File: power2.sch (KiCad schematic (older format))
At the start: 40 parts, among them U3 LMS6002DR2, U4 ECP5

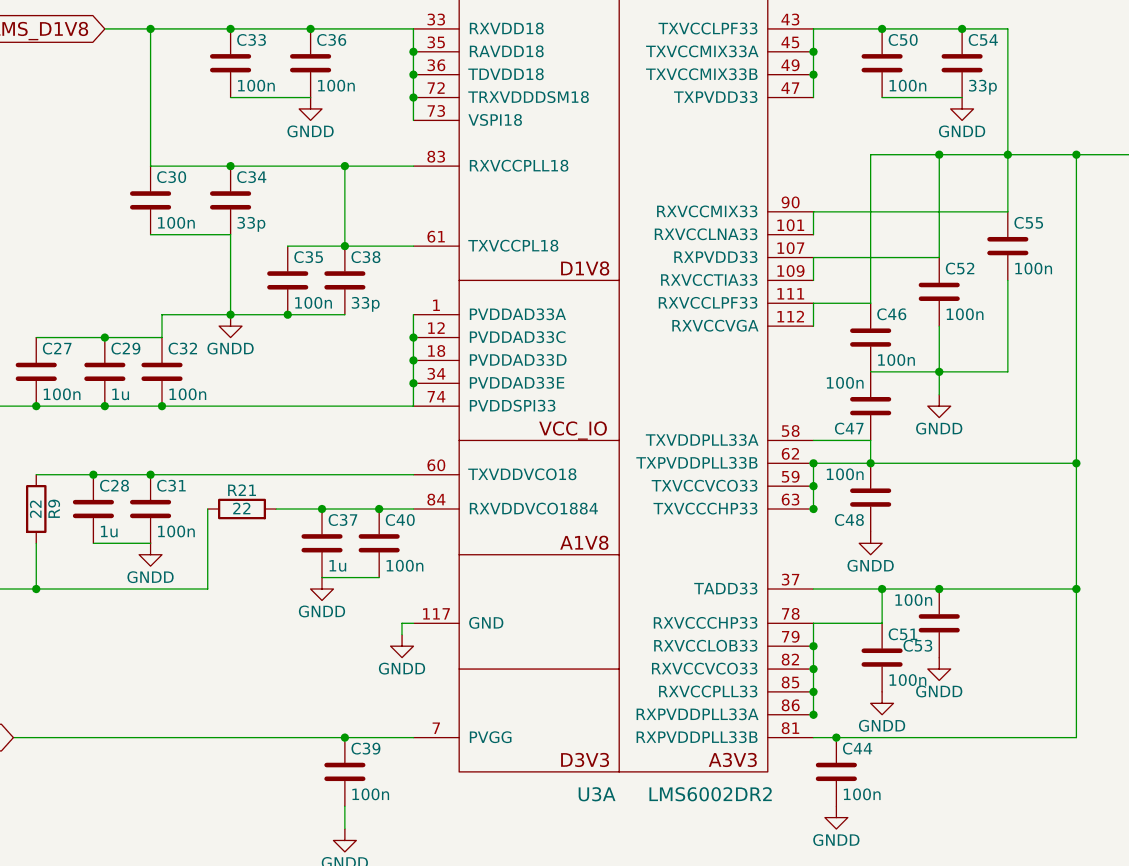
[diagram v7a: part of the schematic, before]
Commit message: Add jumpers for LMS power Traced most nets in LMS digital
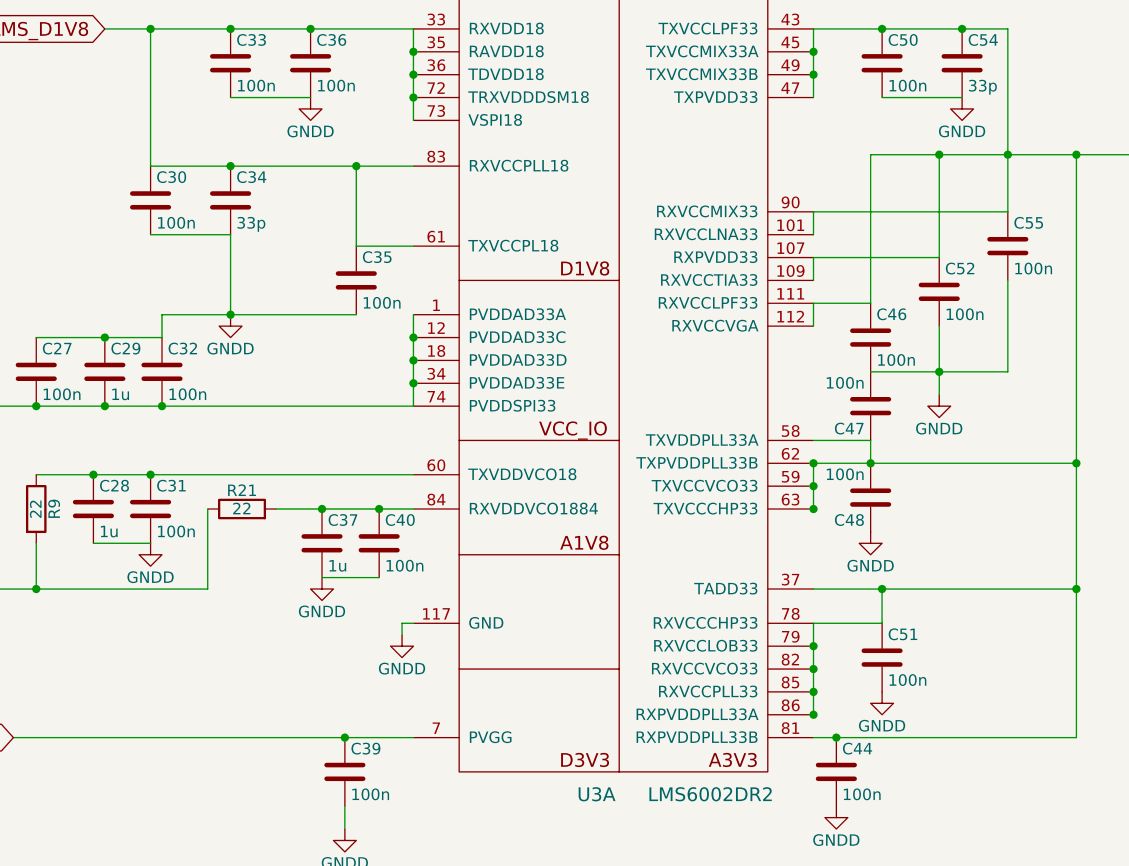
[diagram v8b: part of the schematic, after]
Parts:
- removed C38: 33p, Capacitors_SMD:C_0603, symbol C
- removed C53: 100n, Capacitors_SMD:C_0603, symbol C
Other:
- moved on the sheet: C35
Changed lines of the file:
@@
 Connection ~ 10950 1000
 $Comp
-L GNDD #PWR075
+L GNDD #PWR91
 U 1 1 58A3CB56
 P 10050 6200
-F 0 "#PWR075" H 10050 5950 50  0001 C CNN
+F 0 "#PWR91" H 10050 5950 50  0001 C CNN
 F 1 "GNDD" H 10050 6050 50  0000 C CNN
 F 2 "" H 10050 6200 50  0000 C CNN
@@
 $EndComp
 $Comp
-L +1V1 #PWR076
+L +1V1 #PWR89
 U 1 1 58A3D047
 P 7500 2300
-F 0 "#PWR076" H 7500 2150 50  0001 C CNN
+F 0 "#PWR89" H 7500 2150 50  0001 C CNN
 F 1 "+1V1" H 7500 2440 50  0000 C CNN
 F 2 "" H 7500 2300 50  0000 C CNN
@@
 L C C35
 U 1 1 58A43C62
-P 2500 1950
-F 0 "C35" H 2525 2050 50  0000 L CNN
-F 1 "100n" H 2525 1850 50  0000 L CNN
-F 2 "Capacitors_SMD:C_0603" H 2538 1800 50  0001 C CNN
-F 3 "" H 2500 1950 50  0000 C CNN
-	1    2500 1950
+P 2800 1950
+F 0 "C35" H 2825 2050 50  0000 L CNN
+F 1 "100n" H 2825 1850 50  0000 L CNN
+F 2 "Capacitors_SMD:C_0603" H 2838 1800 50  0001 C CNN
+F 3 "" H 2800 1950 50  0000 C CNN
+	1    2800 1950
 	1    0    0    -1
 $EndComp
@@
 $EndComp
 $Comp
-L C C38
-U 1 1 58A43C77
-P 2750 1950
-F 0 "C38" H 2775 2050 50  0000 L CNN
-F 1 "33p" H 2775 1850 50  0000 L CNN
-F 2 "Capacitors_SMD:C_0603" H 2788 1800 50  0001 C CNN
-F 3 "" H 2750 1950 50  0000 C CNN
-	1    2750 1950
-	1    0    0    -1
-$EndComp
-$Comp
-L GNDD #PWR077
+L GNDD #PWR76
 U 1 1 58A43C7E
 P 2250 2100
-F 0 "#PWR077" H 2250 1850 50  0001 C CNN
+F 0 "#PWR76" H 2250 1850 50  0001 C CNN
 F 1 "GNDD" H 2250 1950 50  0000 C CNN
 F 2 "" H 2250 2100 50  0000 C CNN
@@
 LMS_D1V8
 $Comp
-L GNDD #PWR078
+L GNDD #PWR77
 U 1 1 58A43C85
 P 2600 1150
-F 0 "#PWR078" H 2600 900 50  0001 C CNN
+F 0 "#PWR77" H 2600 900 50  0001 C CNN
 F 1 "GNDD" H 2600 1000 50  0000 C CNN
 F 2 "" H 2600 1150 50  0000 C CNN
@@
 LMS_A1V8
 $Comp
-L GNDD #PWR079
+L GNDD #PWR80
 U 1 1 58A43CCB
 P 3000 3500
-F 0 "#PWR079" H 3000 3250 50  0001 C CNN
+F 0 "#PWR80" H 3000 3250 50  0001 C CNN
 F 1 "GNDD" H 3000 3350 50  0000 C CNN
 F 2 "" H 3000 3500 50  0000 C CNN
@@
 $EndComp
 $Comp
-L GNDD #PWR080
+L GNDD #PWR78
 U 1 1 58A43CD1
 P 2650 3250
-F 0 "#PWR080" H 2650 3000 50  0001 C CNN
+F 0 "#PWR78" H 2650 3000 50  0001 C CNN
 F 1 "GNDD" H 2650 3100 50  0000 C CNN
 F 2 "" H 2650 3250 50  0000 C CNN
@@
 $EndComp
 $Comp
-L GNDD #PWR081
+L GNDD #PWR75
 U 1 1 58A43CD7
 P 1900 3100
-F 0 "#PWR081" H 1900 2850 50  0001 C CNN
+F 0 "#PWR75" H 1900 2850 50  0001 C CNN
 F 1 "GNDD" H 1900 2950 50  0000 C CNN
 F 2 "" H 1900 3100 50  0000 C CNN
@@
 $EndComp
 $Comp
-L GNDD #PWR082
+L GNDD #PWR85
 U 1 1 58A43CEB
 P 5450 1150
-F 0 "#PWR082" H 5450 900 50  0001 C CNN
+F 0 "#PWR85" H 5450 900 50  0001 C CNN
 F 1 "GNDD" H 5450 1000 50  0000 C CNN
 F 2 "" H 5450 1150 50  0000 C CNN
@@
 $EndComp
 $Comp
-L GNDD #PWR083
+L GNDD #PWR79
 U 1 1 58A43D15
 P 2750 4350
-F 0 "#PWR083" H 2750 4100 50  0001 C CNN
+F 0 "#PWR79" H 2750 4100 50  0001 C CNN
 F 1 "GNDD" H 2750 4200 50  0000 C CNN
 F 2 "" H 2750 4350 50  0000 C CNN
@@
 $EndComp
 $Comp
-L GNDD #PWR084
+L GNDD #PWR84
 U 1 1 58A43D1B
 P 5350 2450
-F 0 "#PWR084" H 5350 2200 50  0001 C CNN
+F 0 "#PWR84" H 5350 2200 50  0001 C CNN
 F 1 "GNDD" H 5350 2300 50  0000 C CNN
 F 2 "" H 5350 2450 50  0000 C CNN
@@
 $EndComp
 $Comp
-L GNDD #PWR085
+L GNDD #PWR82
 U 1 1 58A43D2F
 P 5050 3050
-F 0 "#PWR085" H 5050 2800 50  0001 C CNN
+F 0 "#PWR82" H 5050 2800 50  0001 C CNN
 F 1 "GNDD" H 5050 2900 50  0000 C CNN
 F 2 "" H 5050 3050 50  0000 C CNN
@@
 	1    0    0    -1
 $EndComp
-$Comp
-L C C53
-U 1 1 58A43D35
-P 5350 3450
-F 0 "C53" H 5375 3550 50  0000 L CNN
-F 1 "100n" H 5375 3350 50  0000 L CNN
-F 2 "Capacitors_SMD:C_0603" H 5388 3300 50  0001 C CNN
-F 3 "" H 5350 3450 50  0000 C CNN
-	1    5350 3450
-	-1   0    0    1
-$EndComp
 Wire Wire Line
 	1900 1450 3050 1450
 Connection ~ 2250 1450
 Wire Wire Line
-	2500 1800 3050 1800
-Connection ~ 2750 1800
-Wire Wire Line
-	1950 2100 2750 2100
+	1950 2100 2800 2100
 Wire Wire Line
 	2250 2100 2250 1750
-Connection ~ 2500 2100
 Wire Wire Line
 	2250 1750 1900 1750
@@
 	4800 3300 5950 3300
 Connection ~ 5950 2750
-Connection ~ 5350 3300
-$Comp
-L GNDD #PWR086
-U 1 1 58A43D94
-P 5350 3600
-F 0 "#PWR086" H 5350 3350 50  0001 C CNN
-F 1 "GNDD" H 5350 3450 50  0000 C CNN
-F 2 "" H 5350 3600 50  0000 C CNN
-F 3 "" H 5350 3600 50  0000 C CNN
-	1    5350 3600
-	1    0    0    -1
-$EndComp
 $Comp
 L C C44
@@
 Connection ~ 5100 3300
 $Comp
-L GNDD #PWR087
+L GNDD #PWR83
 U 1 1 58A43DAE
 P 5100 3750
-F 0 "#PWR087" H 5100 3500 50  0001 C CNN
+F 0 "#PWR83" H 5100 3500 50  0001 C CNN
 F 1 "GNDD" H 5100 3600 50  0000 C CNN
 F 2 "" H 5100 3750 50  0000 C CNN
@@
 $EndComp
 $Comp
-L GNDD #PWR088
+L GNDD #PWR81
 U 1 1 58A43DB4
 P 4900 4250
-F 0 "#PWR088" H 4900 4000 50  0001 C CNN
+F 0 "#PWR81" H 4900 4000 50  0001 C CNN
 F 1 "GNDD" H 4900 4100 50  0000 C CNN
 F 2 "" H 4900 4250 50  0000 C CNN
@@
 	7500 2300 9450 2300
 $Comp
-L +2V5 #PWR089
+L +2V5 #PWR87
 U 1 1 58A517A0
 P 7300 3300
-F 0 "#PWR089" H 7300 3150 50  0001 C CNN
+F 0 "#PWR87" H 7300 3150 50  0001 C CNN
 F 1 "+2V5" H 7300 3440 50  0000 C CNN
 F 2 "" H 7300 3300 50  0000 C CNN
@@
 $EndComp
 $Comp
-L GNDD #PWR090
+L GNDD #PWR88
 U 1 1 58A51D8C
 P 7300 3800
-F 0 "#PWR090" H 7300 3550 50  0001 C CNN
+F 0 "#PWR88" H 7300 3550 50  0001 C CNN
 F 1 "GNDD" H 7300 3650 50  0000 C CNN
 F 2 "" H 7300 3800 50  0000 C CNN
@@
 Connection ~ 6750 2950
 $Comp
-L GNDD #PWR091
+L GNDD #PWR86
 U 1 1 58A54D9A
 P 6500 3050
-F 0 "#PWR091" H 6500 2800 50  0001 C CNN
+F 0 "#PWR86" H 6500 2800 50  0001 C CNN
 F 1 "GNDD" H 6500 2900 50  0000 C CNN
 F 2 "" H 6500 3050 50  0000 C CNN
@@
 Connection ~ 8650 2300
 $Comp
-L GNDD #PWR092
+L GNDD #PWR90
 U 1 1 58A55DE2
 P 8650 2750
-F 0 "#PWR092" H 8650 2500 50  0001 C CNN
+F 0 "#PWR90" H 8650 2500 50  0001 C CNN
 F 1 "GNDD" H 8650 2600 50  0000 C CNN
 F 2 "" H 8650 2750 50  0000 C CNN
@@
 Connection ~ 8650 2700
 Connection ~ 1400 3300
-Wire Wire Line
-	2750 1800 2750 1450
-Connection ~ 2750 1450
 $Comp
 L C C29
@@
 	1400 2200 1950 2200
 Connection ~ 1700 2200
+Wire Wire Line
+	3050 1800 2800 1800
+Wire Wire Line
+	2800 1800 2800 1450
+Connection ~ 2800 1450
 $EndSCHEMATC
